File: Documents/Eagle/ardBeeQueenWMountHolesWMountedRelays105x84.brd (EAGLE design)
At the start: 109.8 x 89.1 mm, 12 parts

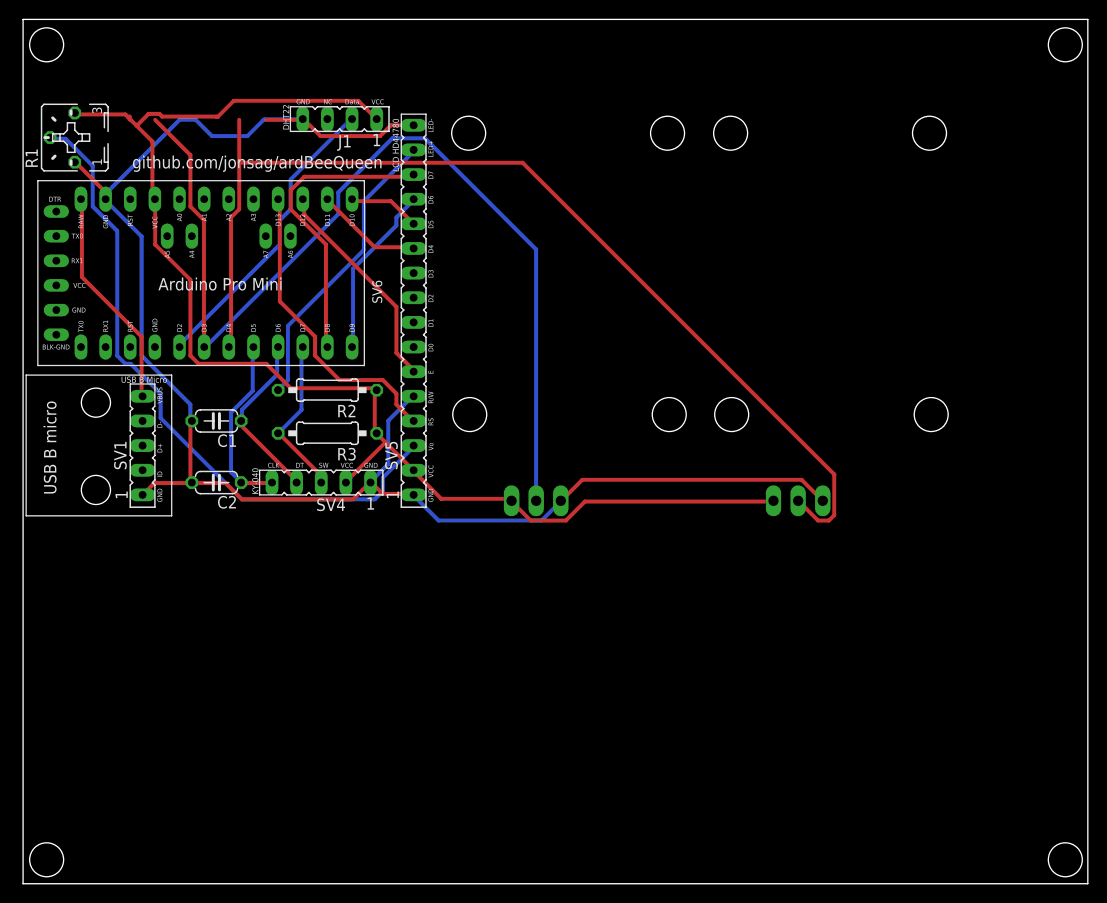
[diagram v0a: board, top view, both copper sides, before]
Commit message: updated eagle docs
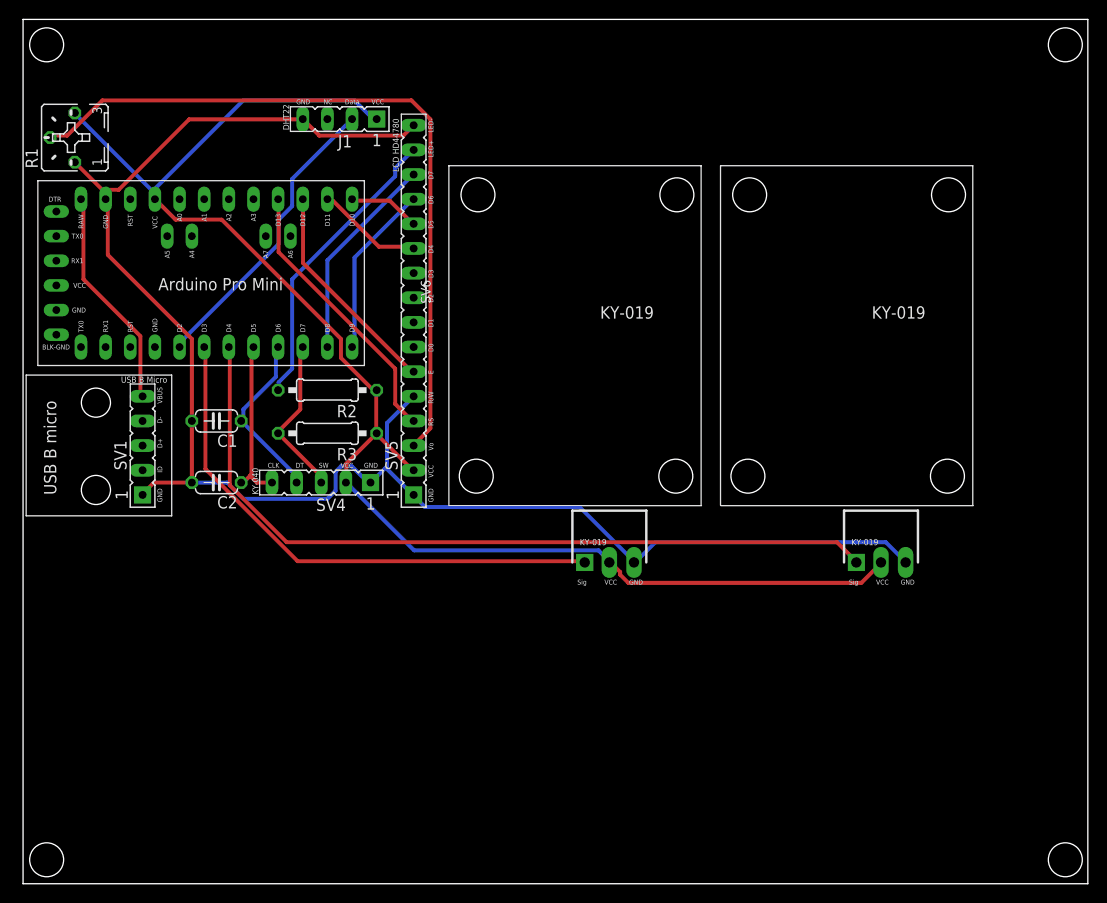
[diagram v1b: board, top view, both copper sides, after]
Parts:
- moved SV7 6.00 mm to (85.0, 54.0)
- moved SV6 5.00 mm to (57.0, 54.0)
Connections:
- net N$1: now also SV5.VO; no longer SV5.3
- net N$10: now also SV4.DT; no longer SV4.4
- net N$11: now also SV4.CLK; no longer SV4.5
- net N$12: now also J1.DATA; no longer J1.2
- net N$13: now also SV6.SIG; no longer SV6.2
- net N$14: now also SV7.SIG; no longer SV7.2
- net N$15: now also J1.VCC, SV4.VCC, SV5.VCC, SV6.VCC, SV7.VCC; no longer J1.1, SV4.2, SV5.2, SV6.3, SV7.3
- net N$16: now also J1.GND, SV1.GND, SV4.GND, SV5.GND, SV5.LED-, SV5.R/W, SV6.GND, SV7.GND; no longer J1.4, SV1.1, SV4.1, SV5.1, SV5.16, SV5.5, SV6.1, SV7.1
- net N$17: now also SV1.VBUS; no longer SV1.5
- net N$2: now also SV5.LED+; no longer SV5.15
- net N$3: now also SV5.D6; no longer SV5.13
- net N$4: now also SV5.D7; no longer SV5.14
- net N$5: now also SV5.D5; no longer SV5.12
- net N$6: now also SV5.D4; no longer SV5.11
- net N$7: now also SV5.E; no longer SV5.6
- net N$8: now also SV5.RS; no longer SV5.4
- net N$9: now also SV4.SW; no longer SV4.3
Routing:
- net N$13: track 100.6 -> 55.8 mm
- net N$14: track 107.5 -> 82.3 mm
- net N$15: track 136.7 -> 150.4 mm
- net N$4: track 31.1 -> 21.5 mm
- net N$1: track 67.5 -> 76.0 mm
- net N$16: track 167.1 -> 173.1 mm
- net N$8: track 31.3 -> 28.7 mm
- net N$11: track 18.6 -> 17.3 mm
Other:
- board text removed: "github.com/jonsag/ardBeeQueen"

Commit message: upd
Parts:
- moved SV5 22.9 mm to (36.8, 55.9)
- moved J1 6.35 mm to (33.0, 93.3)
- moved SV1 6.35 mm to (8.89, 54.6)
- moved SV4 6.35 mm to (32.4, 55.9)
- moved SV7 2.54 mm to (82.5, 54.0)
- moved SV6 2.54 mm to (54.5, 54.0)
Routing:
- net N$16: track 173.1 -> 0.00 mm
- net N$15: track 150.4 -> 0.00 mm
- net N$14: track 82.3 -> 0.00 mm
- net N$1: track 76.0 -> 0.00 mm
- net N$13: track 55.8 -> 0.00 mm
- net N$12: track 30.9 -> 0.00 mm
- net N$2: track 30.5 -> 0.00 mm
- net N$8: track 28.7 -> 0.00 mm
- net N$17: track 23.1 -> 0.00 mm
- net N$7: track 22.6 -> 0.00 mm
- net N$4: track 21.5 -> 0.00 mm
- net N$10: track 18.2 -> 0.00 mm
- net N$3: track 18.0 -> 0.00 mm
- net N$11: track 17.3 -> 0.00 mm
- net N$9: track 17.1 -> 0.00 mm
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
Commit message: added PID sketch
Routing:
- net N$16: track 0.00 -> 170.2 mm
- net N$15: track 0.00 -> 150.5 mm
- net N$14: track 0.00 -> 75.4 mm
- net N$1: track 0.00 -> 74.1 mm
- net N$13: track 0.00 -> 50.6 mm
- net N$2: track 0.00 -> 31.9 mm
- net N$12: track 0.00 -> 30.9 mm
- net N$8: track 0.00 -> 27.4 mm
- net N$17: track 0.00 -> 23.1 mm
- net N$4: track 0.00 -> 22.8 mm
- net N$7: track 0.00 -> 21.3 mm
- net N$3: track 0.00 -> 19.4 mm
- net N$11: track 0.00 -> 18.8 mm
- net N$10: track 0.00 -> 18.2 mm
- net N$9: track 0.00 -> 17.1 mm
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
